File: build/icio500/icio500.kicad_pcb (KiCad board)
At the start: 4 copper layers, 150.8 x 114.3 mm, 56 parts, among them J1 ?, U1 ?, U2 ?, U3 ?, U4 ?, U5 ?, U6 ?

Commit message: Optimize ribbon connector placement on both satellite and main boards for clean ribbon routing
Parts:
- moved U6 16.5 mm to (93.4, 123.5)
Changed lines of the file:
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@@
 	(footprint "Connector_PinHeader_2.54mm:PinHeader_2x10_P2.54mm_Vertical"
 		(layer "F.Cu")
-		(at 93.37 107 90)
+		(at 93.37 123.475 90)
 		(descr "Through hole straight pin header, 2x10, 2.54mm pitch, double rows")
 		(tags "Through hole pin header THT 2x10 2.54mm double row")

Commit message: Fix orientation of ribbon connectors to prevent them from hanging off the PCB
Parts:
- turned U6 to 0 degrees
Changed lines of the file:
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@@
 	(footprint "Connector_PinHeader_2.54mm:PinHeader_2x10_P2.54mm_Vertical"
 		(layer "F.Cu")
-		(at 93.37 123.475 90)
+		(at 93.37 123.475 0)
 		(descr "Through hole straight pin header, 2x10, 2.54mm pitch, double rows")
 		(tags "Through hole pin header THT 2x10 2.54mm double row")

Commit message: Refactor mechanical assembly: Use direct right-angle header connection between main board and satellite board, eliminating the ribbon cable
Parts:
- U6: footprint Connector_PinHeader_2.54mm:PinHeader_2x10_P2.54mm_Vertical -> Connector_PinHeader_2.54mm:PinHeader_2x10_P2.54mm_Horizontal
- moved U6 41.3 mm to (52.2, 120.5), turned to 180 degrees
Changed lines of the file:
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@@
 		)
 	)
-	(footprint "Connector_PinHeader_2.54mm:PinHeader_2x10_P2.54mm_Vertical"
+	(footprint "Connector_PinHeader_2.54mm:PinHeader_2x10_P2.54mm_Horizontal"
 		(layer "F.Cu")
-		(at 93.37 123.475 0)
+		(at 52.17 120.475 180)
 		(descr "Through hole straight pin header, 2x10, 2.54mm pitch, double rows")
 		(tags "Through hole pin header THT 2x10 2.54mm double row")
@@
 		)
 		(embedded_fonts no)
-		(model "${KICAD10_3DMODEL_DIR}/Connector_PinHeader_2.54mm.3dshapes/PinHeader_2x10_P2.54mm_Vertical.step"
+		(model "/Connector_PinHeader_2.54mm.3dshapes/PinHeader_2x10_P2.54mm_Horizontal.step"
 			(offset
 				(xyz 0 0 0)

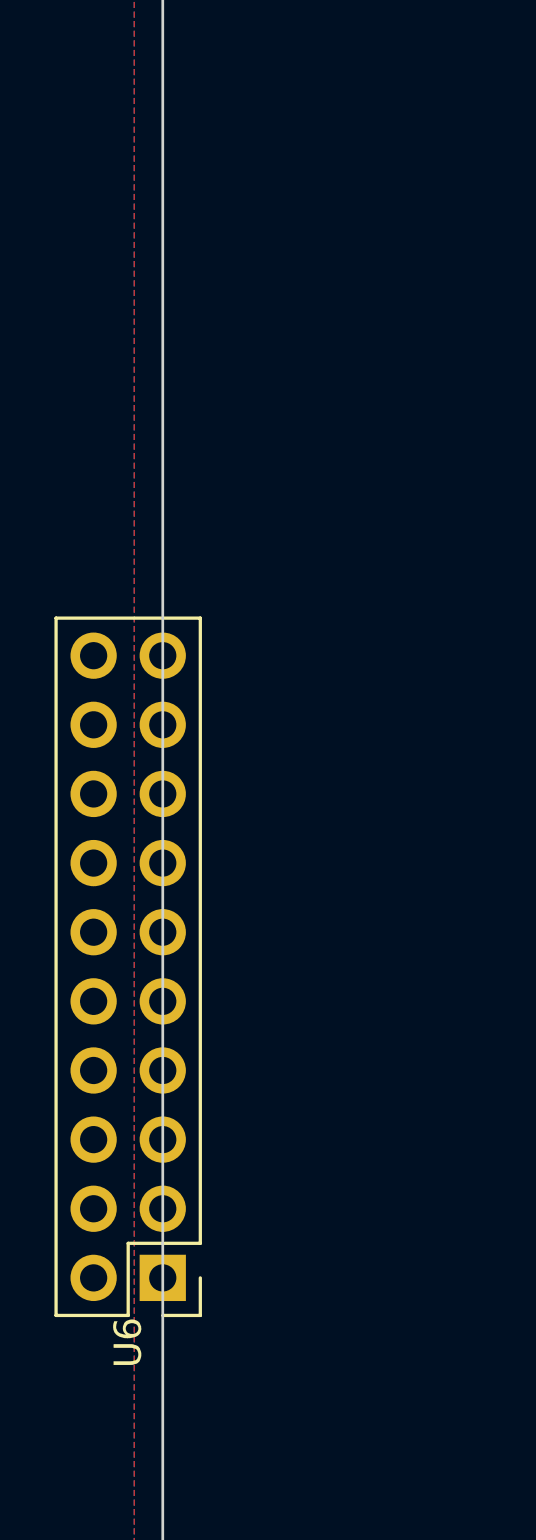
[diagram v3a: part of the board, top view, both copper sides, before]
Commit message: Fix final mechanical alignments: Sync assembly file, fix U6 Y-axis inversion, use exact zero-origin STEP exports
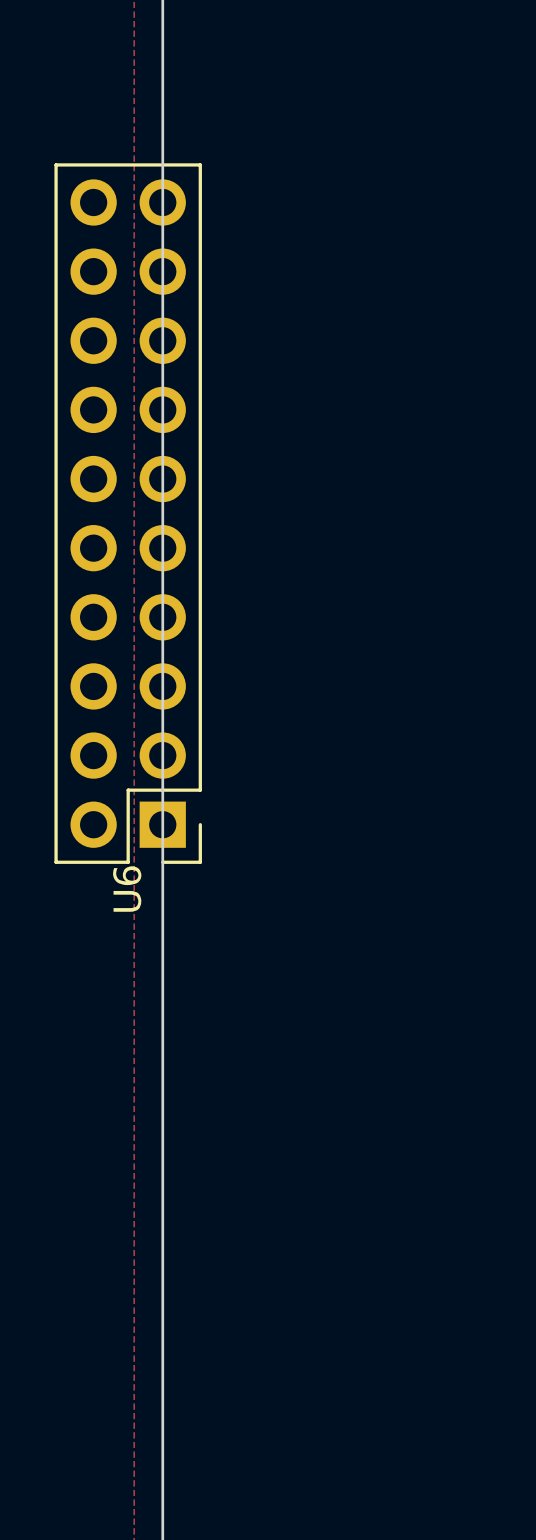
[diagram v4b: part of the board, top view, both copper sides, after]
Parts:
- moved U6 16.6 mm to (52.2, 103.8)
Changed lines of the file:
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@@
 	(footprint "Connector_PinHeader_2.54mm:PinHeader_2x10_P2.54mm_Horizontal"
 		(layer "F.Cu")
-		(at 52.17 120.475 180)
+		(at 52.17 103.825 180)
 		(descr "Through hole straight pin header, 2x10, 2.54mm pitch, double rows")
 		(tags "Through hole pin header THT 2x10 2.54mm double row")

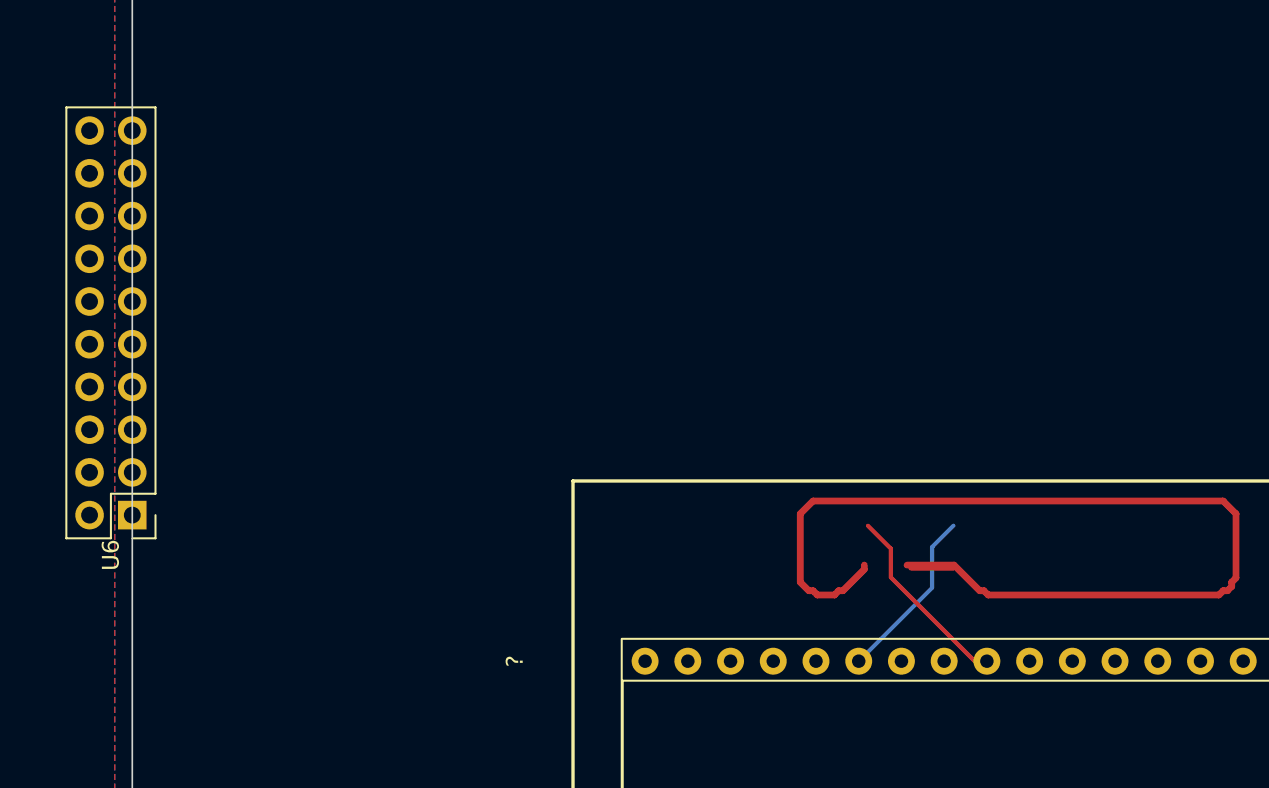
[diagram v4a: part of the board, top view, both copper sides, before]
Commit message: Fix 3D offsets finally (Offset AFTER rotation) and autoroute main board U6 connections
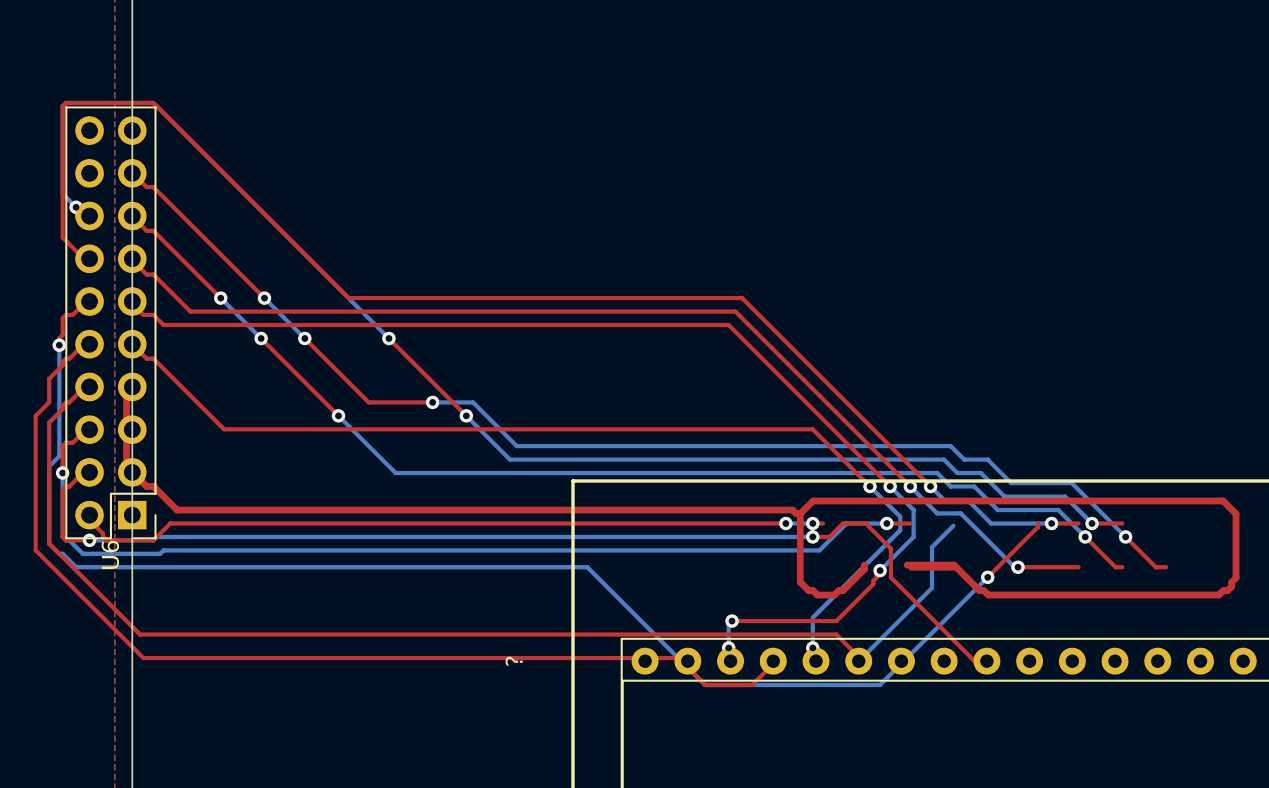
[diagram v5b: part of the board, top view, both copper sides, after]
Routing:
- net spi1_mosi: track 8.87 -> 91.0 mm
- net spi1_sck: track 9.93 -> 90.7 mm
- net gpio_disp_dc: track 11.4 -> 92.2 mm
- net gpio_disp_res: track 9.35 -> 80.7 mm
- net gpio_enc_sw: track 20.6 -> 89.3 mm
- net spi1_cs: track 7.39 -> 75.1 mm
- net spi1_miso: track 6.33 -> 70.4 mm
- net gpio_enc_b: track 17.1 -> 79.1 mm
- net d13: track 10.4 -> 71.9 mm
- net d14: track 14.4 -> 75.1 mm
- net i2c1_scl: track 16.0 -> 75.0 mm
- net i2c1_sda: track 11.4 -> 64.6 mm
- net gnd: track 223.5 -> 269.1 mm
- net audio_in_r: track 49.6 -> 94.6 mm
- net 0: vias 0 -> 30

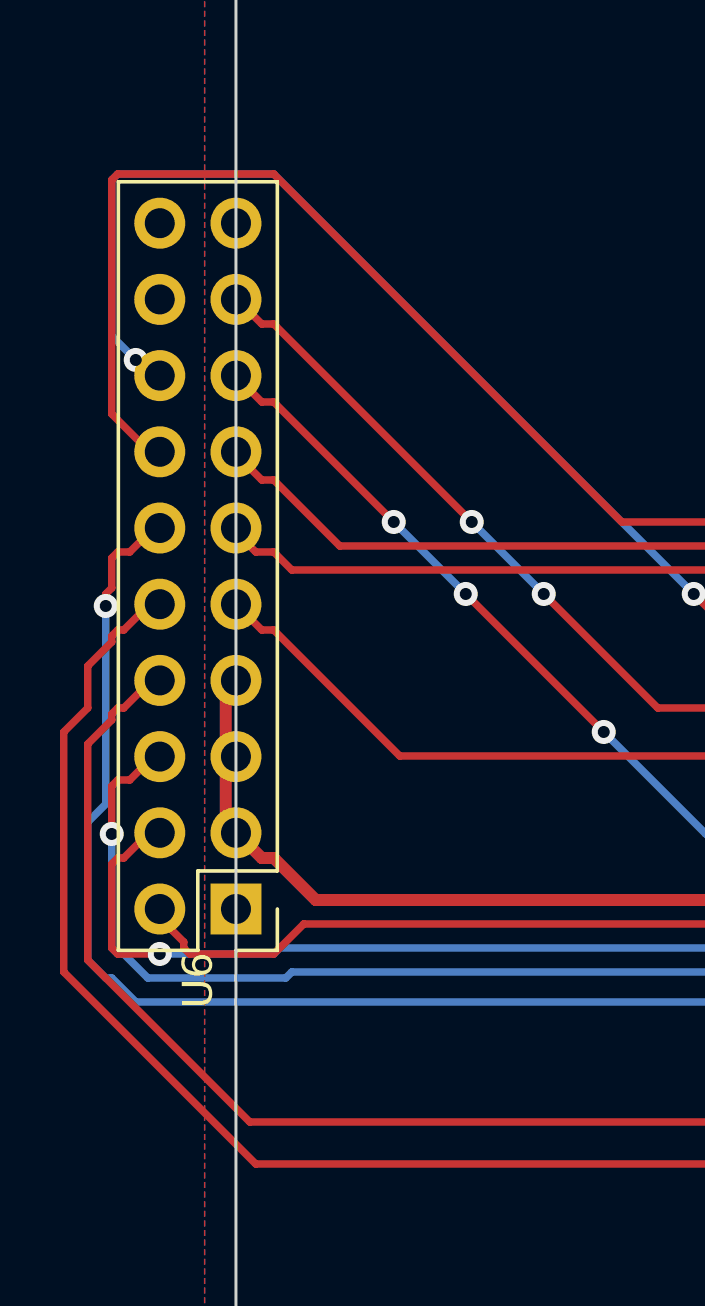
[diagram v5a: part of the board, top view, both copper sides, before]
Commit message: Move U6 to X=56.0, reconnect perfectly, and finalize exact GUI 3D offsets
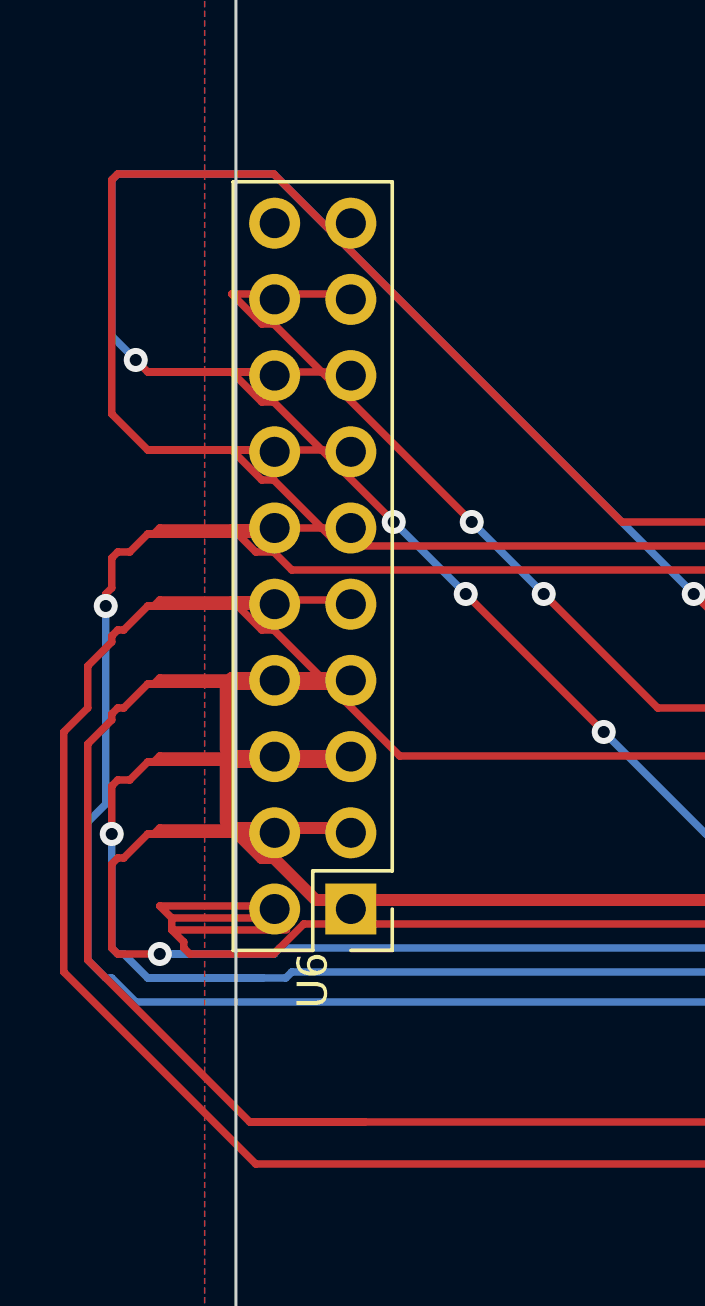
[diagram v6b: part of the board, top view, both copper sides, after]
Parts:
- moved U6 3.83 mm to (56.0, 103.8)
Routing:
- net gnd: track 269.1 -> 288.3 mm
- net i2c1_sda: track 64.6 -> 79.9 mm
- net i2c1_scl: track 75.0 -> 90.3 mm
- net d13: track 71.9 -> 87.3 mm
- net spi1_mosi: track 91.0 -> 102.5 mm
- net gpio_enc_b: track 79.1 -> 90.6 mm
- net audio_in_r: track 94.6 -> 106.1 mm
- net gpio_disp_dc: track 92.2 -> 99.8 mm
- net spi1_sck: track 90.7 -> 98.3 mm
- net gpio_disp_res: track 80.7 -> 84.6 mm
- net spi1_miso: track 70.4 -> 74.2 mm
- net spi1_cs: track 75.1 -> 78.9 mm
- net gpio_enc_sw: track 89.3 -> 93.2 mm
- net d14: track 75.1 -> 78.9 mm

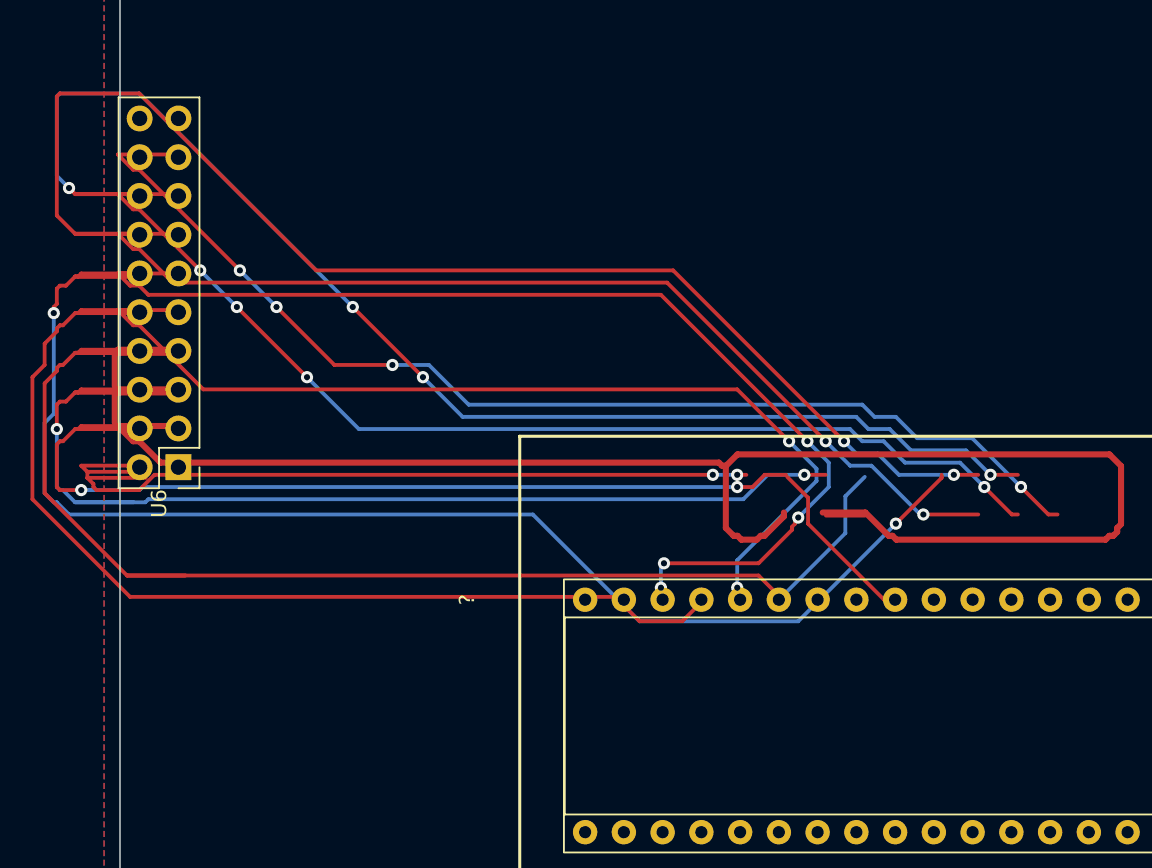
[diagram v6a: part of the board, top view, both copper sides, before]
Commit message: Fix mechanical alignment, restore routing to 0 unconnected nets
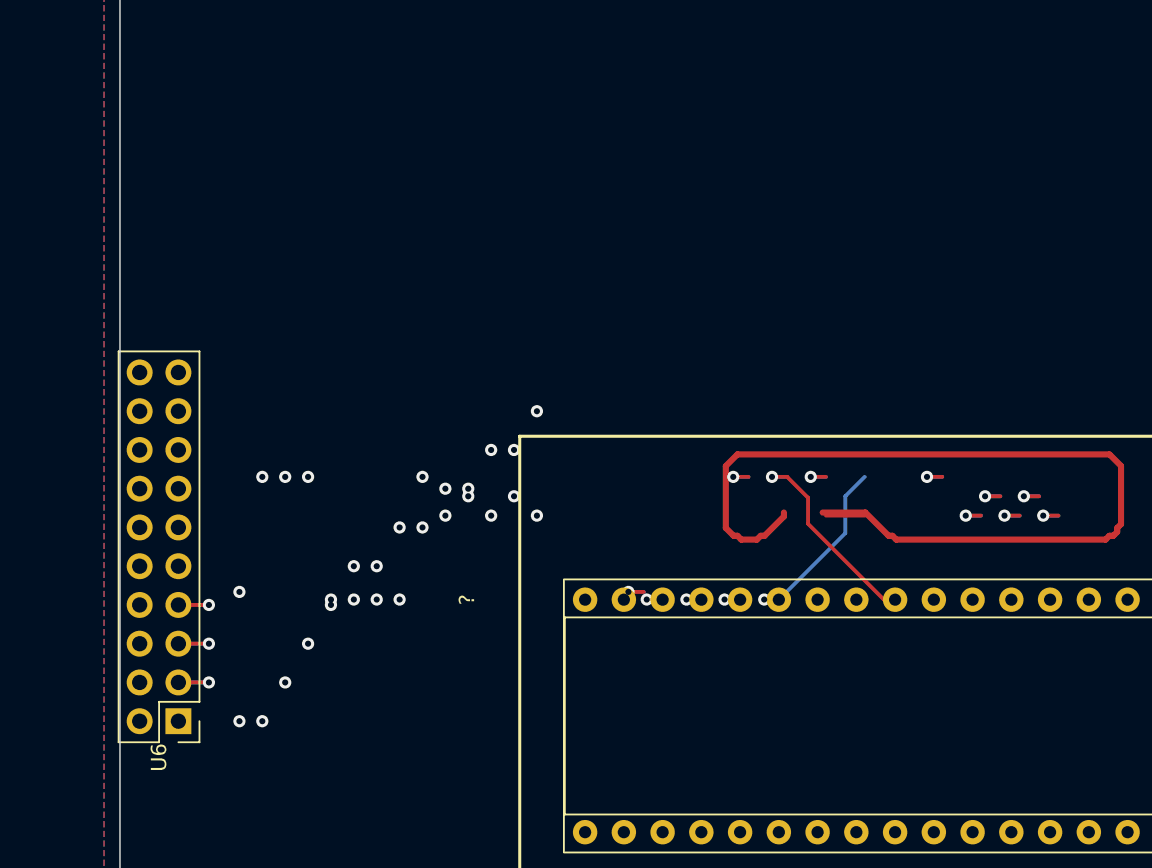
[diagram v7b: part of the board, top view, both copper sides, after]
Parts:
- moved U6 16.6 mm to (56.0, 120.5)
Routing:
- net gnd: track 288.3 -> 235.5 mm, vias 22 -> 25
- net daisy_5v_power: track 113.1 -> 155.1 mm, vias 0 -> 3
- net spi1_mosi: track 102.5 -> 67.8 mm, vias 0 -> 3
- net gpio_enc_sw: track 93.2 -> 60.0 mm, vias 0 -> 3
- net d13: track 87.3 -> 55.7 mm, vias 0 -> 3
- net gpio_enc_b: track 90.6 -> 59.1 mm, vias 0 -> 3
- net spi1_sck: track 98.3 -> 69.8 mm, vias 0 -> 3
- net gpio_disp_dc: track 99.8 -> 76.4 mm, vias 0 -> 3
- net d14: track 78.9 -> 56.4 mm, vias 0 -> 3
- net i2c1_scl: track 90.3 -> 74.9 mm, vias 0 -> 3
- net spi1_miso: track 74.2 -> 63.7 mm, vias 0 -> 3
- net i2c1_sda: track 79.9 -> 70.3 mm, vias 0 -> 3
- net spi1_cs: track 78.9 -> 69.8 mm, vias 0 -> 3
- net gpio_disp_res: track 84.6 -> 76.9 mm, vias 0 -> 3
- net audio_in_r: track 106.1 -> 108.5 mm, vias 0 -> 3
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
